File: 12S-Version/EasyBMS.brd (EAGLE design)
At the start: 49 x 100 mm, 153 parts, among them IC1 LM2596S-5.0_NOPB, IC2 LTC6811IG-1#PBF, Q10 BSS84LT1G, Q11 BSS84LT1G, Q12 BSS84LT1G, Q13 BSS84LT1G, Q2 BSS84LT1G, Q3 BSS84LT1G, Q4 BSS84LT1G, Q5 BSS84LT1G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

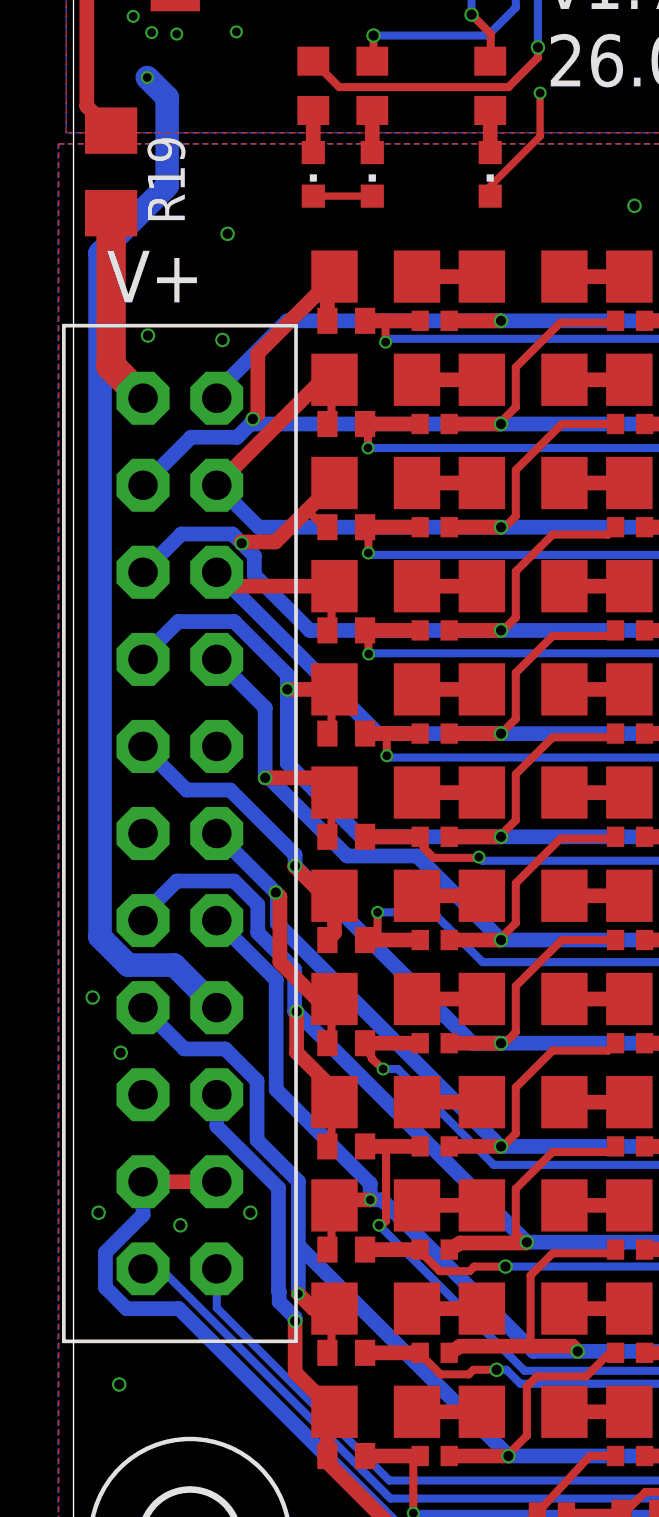
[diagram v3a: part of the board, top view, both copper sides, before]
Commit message: pin distance battery connector changed to 2.7mm
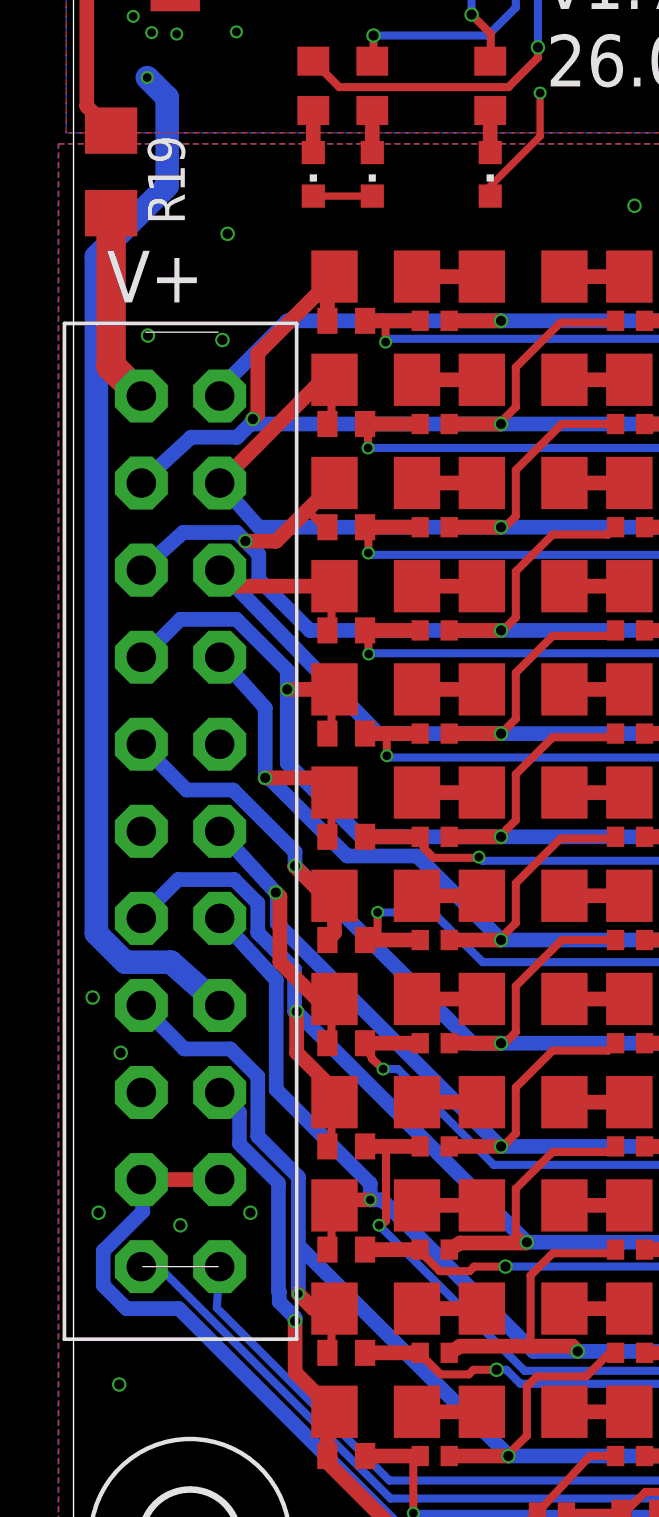
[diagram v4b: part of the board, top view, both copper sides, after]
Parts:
- moved JP7 0.08 mm to (3.69, 28.4)

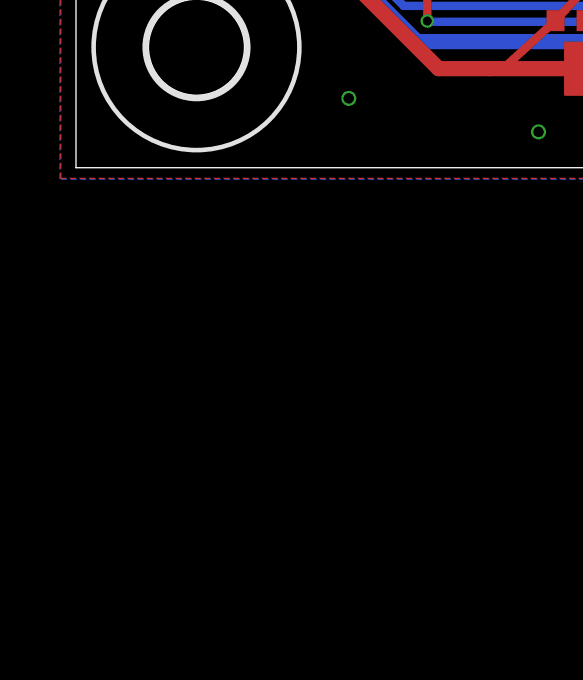
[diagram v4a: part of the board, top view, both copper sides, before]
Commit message: level shifter base design added
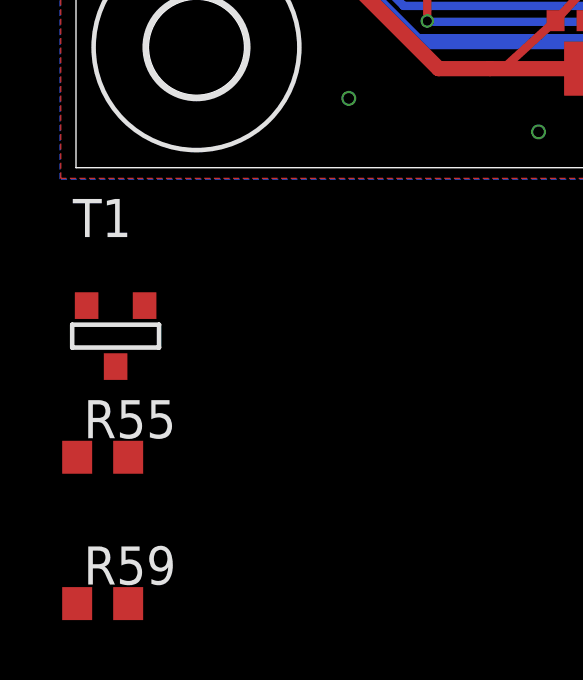
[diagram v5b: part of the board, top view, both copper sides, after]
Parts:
- added R55, R59: 10k, rcl:R0603
- added T1: C8545, zetex:SOT-23
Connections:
- new net N$18: R59.2
- new net N$5: R55.2, T1.3
- new net N$6: R55.1, T1.2
- new net N$7: R59.1, T1.1
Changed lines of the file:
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@@
 <attribute name="VALUE" x="47.4472" y="64.7192" size="1.27" layer="27" rot="R180"/>
+</element>
+<element name="T1" library="zetex" library_urn="urn:adsk.eagle:library:418" package="SOT-23" package3d_urn="urn:adsk.eagle:package:30981/1" value="C8545" x="1.2954" y="-5.6134" smashed="yes">
+<attribute name="MF" value="" x="1.2954" y="-5.6134" size="1.778" layer="27" display="off"/>
+<attribute name="MPN" value="" x="1.2954" y="-5.6134" size="1.778" layer="27" display="off"/>
+<attribute name="NAME" x="-0.1016" y="-2.3114" size="1.27" layer="25" ratio="10"/>
+<attribute name="OC_FARNELL" value="unknown" x="1.2954" y="-5.6134" size="1.778" layer="27" display="off"/>
+<attribute name="OC_NEWARK" value="unknown" x="1.2954" y="-5.6134" size="1.778" layer="27" display="off"/>
+<attribute name="VALUE" x="-0.1016" y="-3.8354" size="1.27" layer="27" ratio="10"/>
+</element>
+<element name="R55" library="rcl" library_urn="urn:adsk.eagle:library:334" package="R0603" package3d_urn="urn:adsk.eagle:package:23555/3" value="10k" x="0.889" y="-9.652" smashed="yes">
+<attribute name="NAME" x="0.254" y="-9.017" size="1.27" layer="25"/>
+<attribute name="POPULARITY" value="70" x="0.889" y="-9.652" size="1.778" layer="27" display="off"/>
+<attribute name="SPICEPREFIX" value="R" x="0.889" y="-9.652" size="1.778" layer="27" display="off"/>
+<attribute name="VALUE" x="0.254" y="-11.557" size="1.27" layer="27"/>
+</element>
+<element name="R59" library="rcl" library_urn="urn:adsk.eagle:library:334" package="R0603" package3d_urn="urn:adsk.eagle:package:23555/3" value="10k" x="0.889" y="-14.5288" smashed="yes">
+<attribute name="NAME" x="0.254" y="-13.8938" size="1.27" layer="25"/>
+<attribute name="POPULARITY" value="70" x="0.889" y="-14.5288" size="1.778" layer="27" display="off"/>
+<attribute name="SPICEPREFIX" value="R" x="0.889" y="-14.5288" size="1.778" layer="27" display="off"/>
+<attribute name="VALUE" x="0.254" y="-16.4338" size="1.27" layer="27"/>
 </element>
 </elements>
@@
 <wire x1="10.2944" y1="50.2718" x2="8.2624" y2="50.2718" width="0.254" layer="1"/>
 </signal>
+<signal name="N$5">
+<contactref element="R55" pad="2"/>
+<contactref element="T1" pad="3"/>
+<wire x1="2.286" y1="-4.5974" x2="1.739" y2="-9.652" width="0" layer="19" extent="1-1"/>
+</signal>
+<signal name="N$6">
+<contactref element="R55" pad="1"/>
+<contactref element="T1" pad="2"/>
+<wire x1="0.3556" y1="-4.5974" x2="0.039" y2="-9.652" width="0" layer="19" extent="1-1"/>
+</signal>
+<signal name="N$7">
+<contactref element="T1" pad="1"/>
+<contactref element="R59" pad="1"/>
+<wire x1="1.3208" y1="-6.6294" x2="0.039" y2="-14.5288" width="0" layer="19" extent="1-1"/>
+</signal>
+<signal name="N$18">
+<contactref element="R59" pad="2"/>
+</signal>
 </signals>

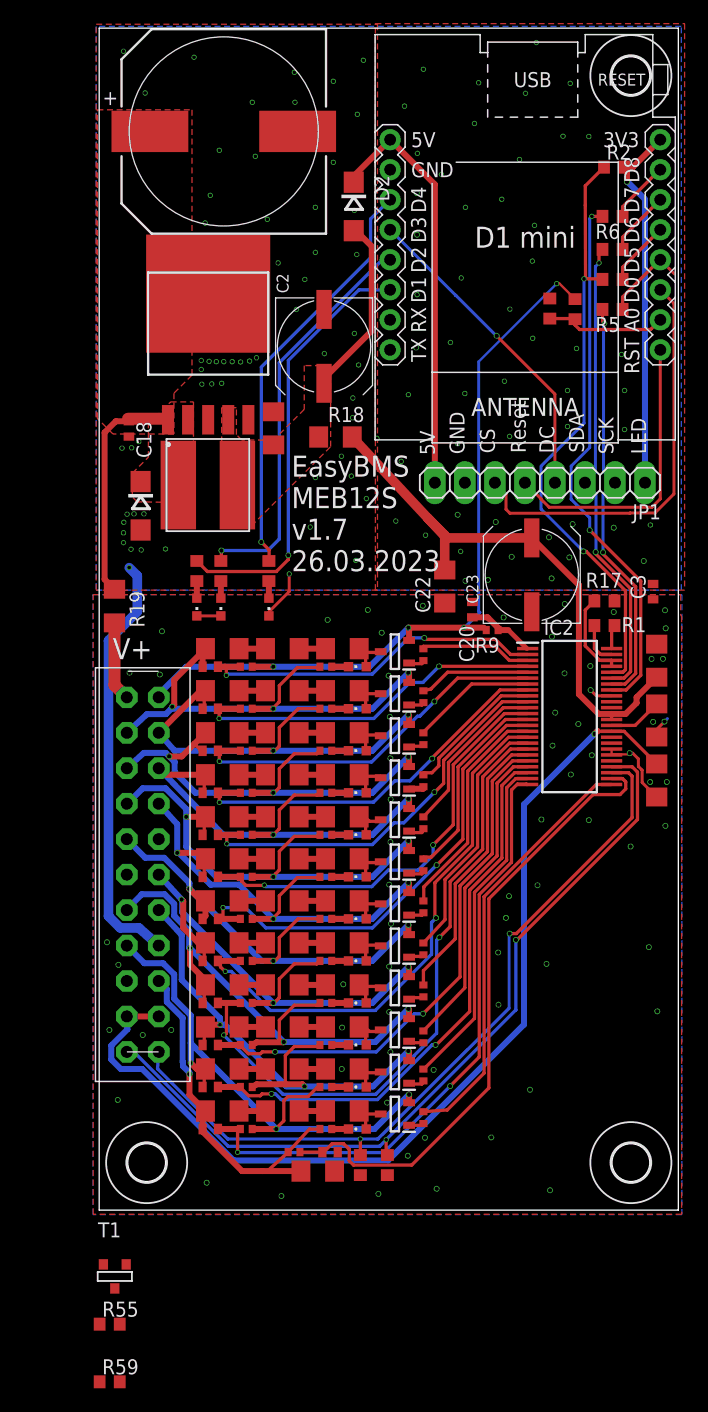
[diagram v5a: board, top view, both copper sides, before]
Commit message: paneled boards removed
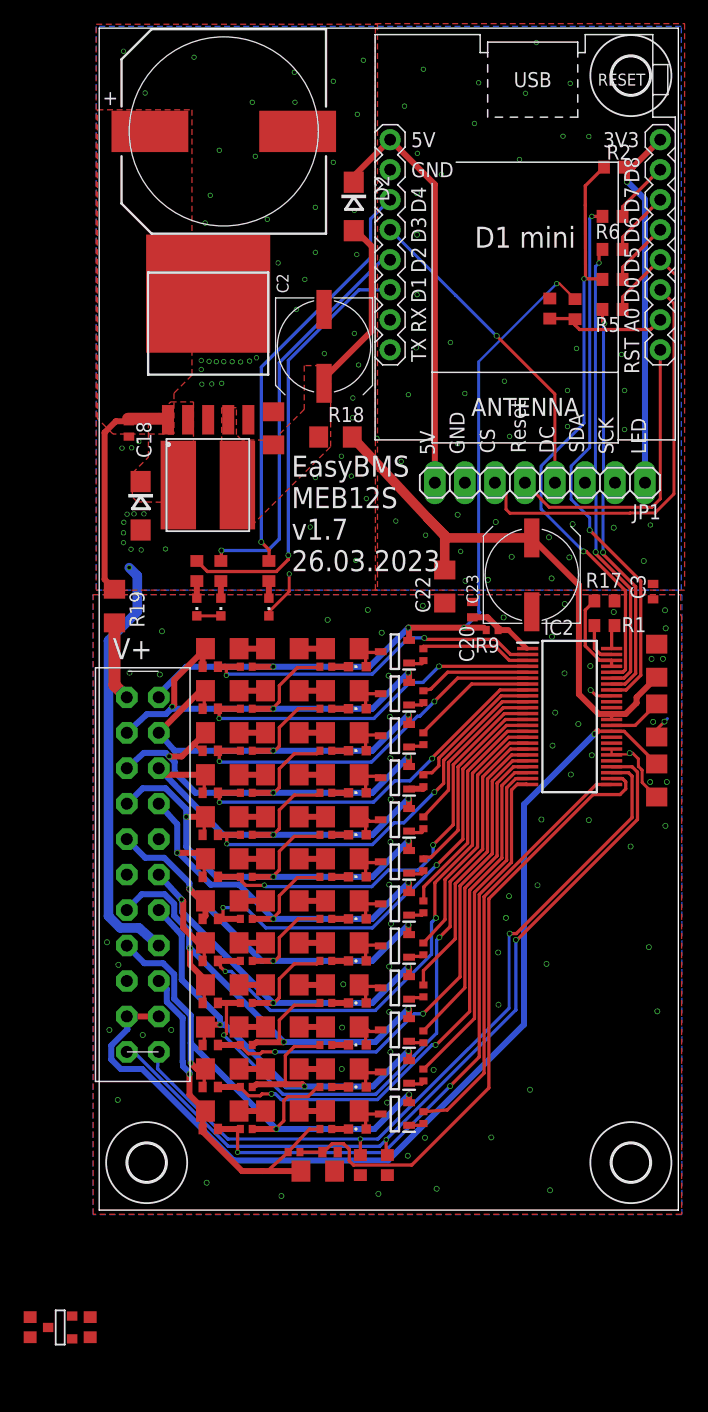
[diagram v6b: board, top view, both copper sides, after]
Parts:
- moved R59 8.17 mm to (-5.84, -9.91), turned to 90 degrees
- moved T1 6.29 mm to (-3.30, -9.91), turned to 270 degrees
- moved R55 1.67 mm to (-0.76, -9.91), turned to 270 degrees
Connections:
- removed net N$18: R59.2
- removed net N$5: R55.2, T1.3
- net +3V3: now also R55.2, T1.3
- net 5VINESP: now also R59.2
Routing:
- net GND: vias 111 -> 104

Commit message: level shifter 3,3V<>5V added
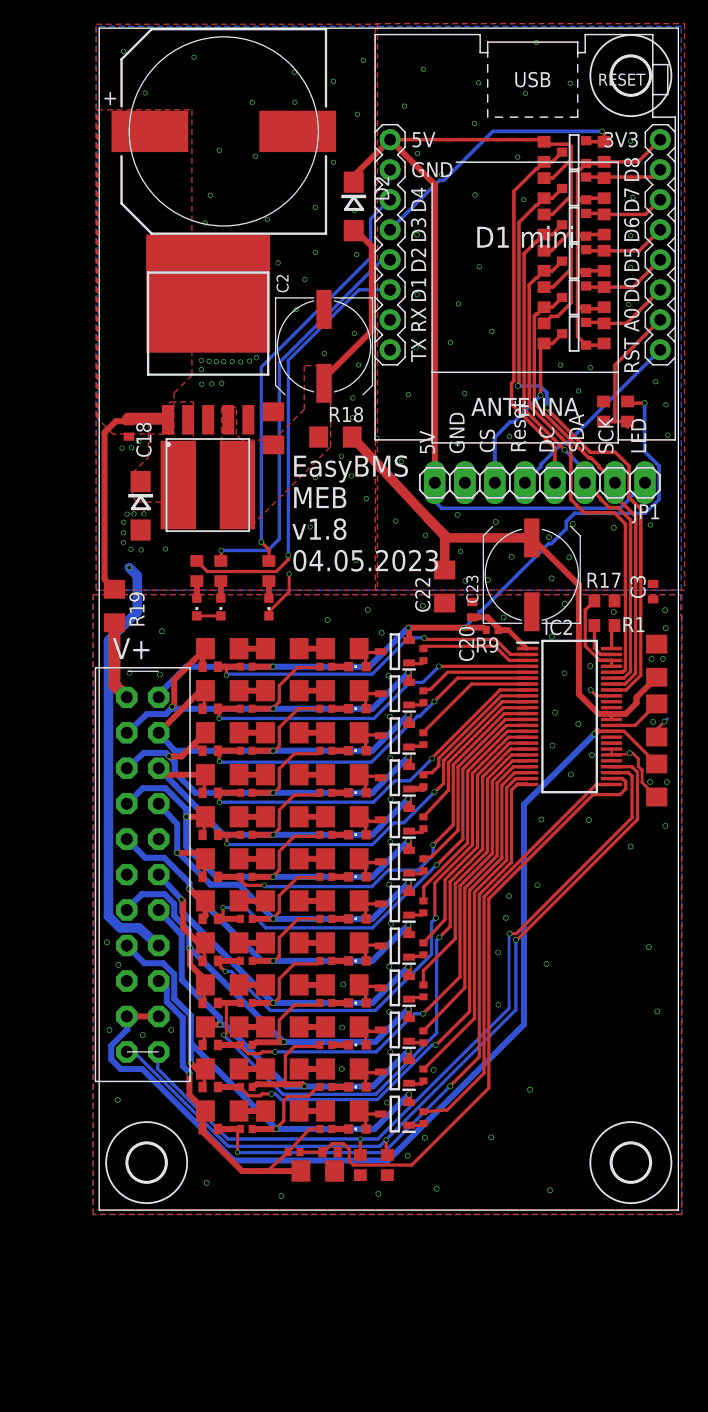
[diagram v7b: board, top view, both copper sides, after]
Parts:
- removed R2: 5K1, rcl:R0603
- removed R5, R6, R61, R62: 1k, rcl:R0603
- added R100, R101, R102, R103, R60, R82, R96, R97, R98, R99: 10k, rcl:R0603
- added T2, T3, T4, T5, T6: C8545, zetex:SOT-23
- moved R55 97.4 mm to (42.7, 77.2)
- moved R59 97.4 mm to (37.6, 77.2)
- moved T1 97.4 mm to (40.2, 77.2)
- moved R16 9.83 mm to (42.7, 67.6)
- moved R15 9.74 mm to (44.7, 67.6)
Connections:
- removed net D0: JP1.6, U$2.JP1.3
- removed net N$15: R6.1, U$2.JP1.7
- removed net N$6: R55.1, T1.2
- removed net N$7: R59.1, T1.1
- removed net N$73: R61.1, U$2.JP1.5
- new net A0DC: JP1.4, R101.1, T5.1
- new net CSDSPL: JP1.6, R103.1, T6.1
- new net CSDSPLESP: R102.1, T6.2, U$2.JP1.3
- new net CSLTCESP: R98.1, T4.2, U$2.JP1.7
- new net MISOESP: R60.1, T2.2, U$2.JP1.5
- net +3V3: now also R100.2, R102.2, R60.2, R96.2, R98.2, T2.3, T3.3, T4.3, T5.3, T6.3; no longer JP1.1, R2.2
- net 5VINESP: now also JP1.1, R101.2, R103.2, R82.2, R97.2, R99.2
- net CSB: now also R99.1, T4.1; no longer R6.2
- net D3: now also R100.1, T5.2; no longer JP1.4
- net MISO: now also R82.1, T2.1; no longer R2.1, R61.2
- net MOSI: now also R97.1, T3.1; no longer R62.2
- net MOSIESP: now also R96.1, T3.2; no longer R62.1
- net SCK: now also R59.1, T1.1; no longer R5.2
- net SCKESP: now also R55.1, T1.2; no longer R5.1
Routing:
- net 5VINESP: track 35.5 -> 99.6 mm
- net D0: track 35.4 -> 0.00 mm
- net A0DC: track 0.00 -> 31.7 mm
- net CSDSPL: track 0.00 -> 15.5 mm, vias 0 -> 1
- net RESET: track 25.2 -> 16.2 mm
- net MISO: track 50.7 -> 42.3 mm, vias 2 -> 0
- net CSDSPLESP: track 0.00 -> 7.49 mm
- net MISOESP: track 0.00 -> 7.05 mm
- net CSB: track 45.9 -> 52.8 mm
- net CSLTCESP: track 0.00 -> 6.66 mm
- net MOSI: track 39.8 -> 45.6 mm, vias 2 -> 1
- net N$73: track 5.53 -> 0.00 mm
- net N$15: track 5.30 -> 0.00 mm
- net SCK: track 35.3 -> 39.3 mm, vias 2 -> 0
- net D3: track 27.3 -> 23.9 mm
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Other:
- board text added: "EasyBMS MEB v1.8 04.05.2023"
- board text removed: "EasyBMS MEB12S v1.7 26.03.2023"
